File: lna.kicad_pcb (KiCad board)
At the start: 2 copper layers, 50.5 x 40.5 mm, 21 parts, among them P1 CONN_1, P2 CONN_2, P3 CONN_1, P4 CONN_1, Q1 BFG540W, U1 LM7810CT

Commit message: Optimizes the layout
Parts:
- Q1: footprint w_smd_trans:sot143B -> bfg540w:sot143B
- moved C3 11.7 mm to (125.1, 116.2), turned to 180 degrees
- moved L2 5.99 mm to (135.3, 106.7), turned to 0 degrees
- moved C1 5.12 mm to (125.1, 106.7), turned to 180 degrees
- moved C2 4.07 mm to (128.9, 94.0)
- moved U1 4.07 mm to (137.2, 95.9)
- moved R3 3.24 mm to (148.0, 104.8)
- moved L3 3.18 mm to (145.4, 108.0)
- moved C5 3.17 mm to (145.4, 94.0)
- moved C6 1.80 mm to (145.4, 111.8)
- moved R1 1.80 mm to (141.0, 111.8)
- moved R2 1.80 mm to (143.5, 111.8)
- moved P2 1.27 mm to (118.1, 94.0)
- moved C4 0.90 mm to (134.0, 112.4), turned to 270 degrees
- moved L1 0.90 mm to (128.9, 112.4), turned to 270 degrees
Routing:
- net GND: track 5.00 -> 164.1 mm
- net Net-(C4-Pad1): track 8.57 -> 3.52 mm
- net Net-(C1-Pad2): track 9.33 -> 4.73 mm
- net Net-(C8-Pad2): track 8.32 -> 4.00 mm
- net Net-(C6-Pad2): track 19.1 -> 15.3 mm
- net VCC: track 16.5 -> 19.6 mm
- net Net-(C1-Pad1): track 8.57 -> 5.77 mm
- net Net-(L2-Pad2): track 9.14 -> 11.2 mm
- net Net-(C3-Pad1): track 10.1 -> 12.0 mm
- net (no net): track 1.61 -> 0.00 mm, vias 1 -> 0

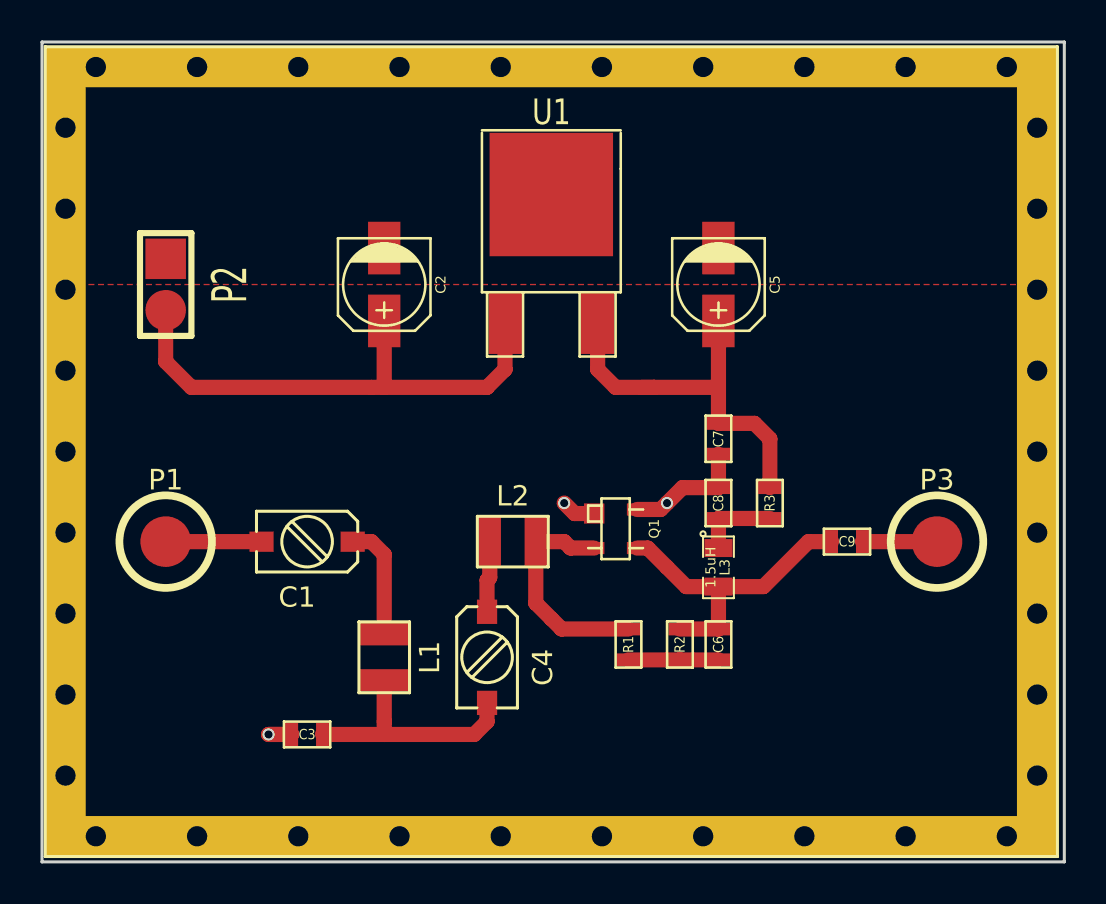
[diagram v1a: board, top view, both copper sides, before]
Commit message: Those are called LC filters not CL filters ... D'oh
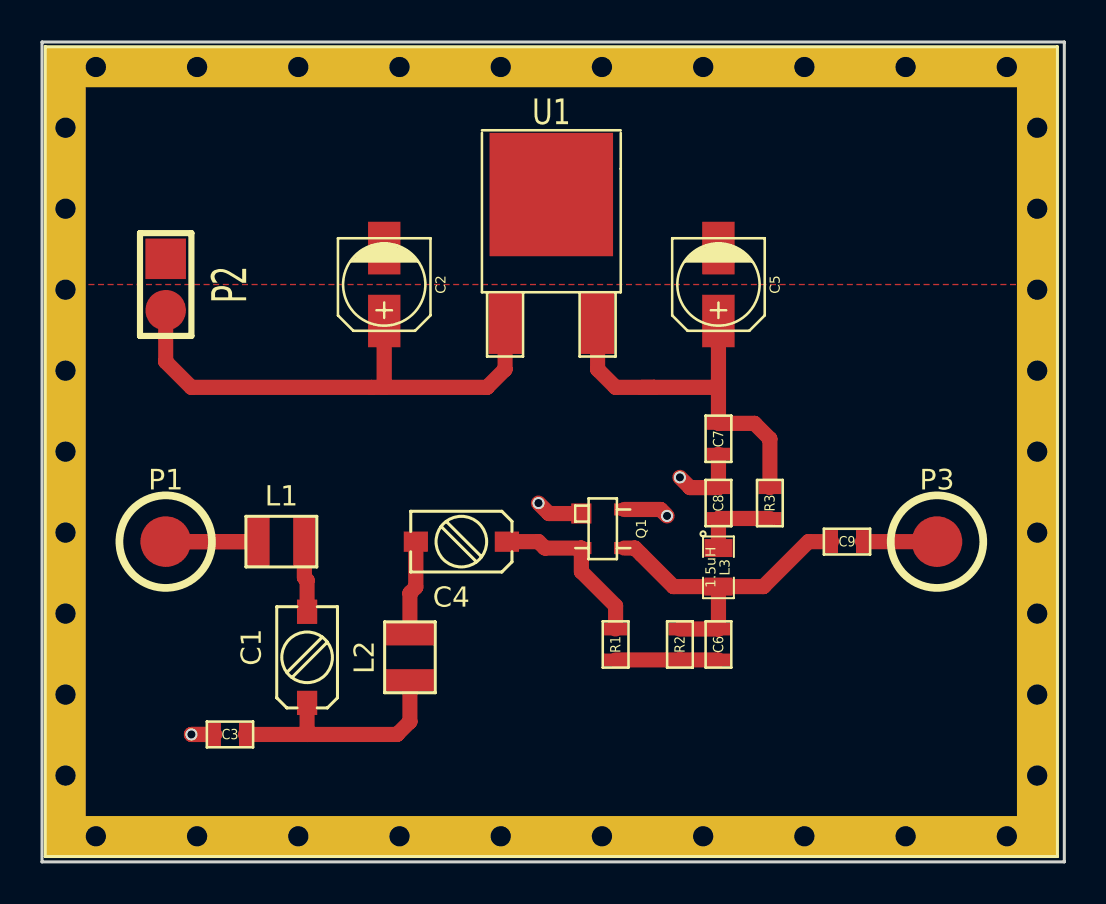
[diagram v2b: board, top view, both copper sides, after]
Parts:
- L1, L2: value 400nH -> 470nH
- moved L1 7.65 mm to (123.8, 106.7), turned to 0 degrees
- moved L2 7.65 mm to (130.2, 112.4), turned to 90 degrees
- moved C4 5.85 mm to (132.7, 106.7), turned to 180 degrees
- moved C1 5.71 mm to (125.1, 112.4), turned to 90 degrees
- moved C3 3.81 mm to (121.3, 116.2)
- moved Q1 0.64 mm to (139.7, 106.0)
- moved R1 0.63 mm to (140.3, 111.8)
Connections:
- C3 pad 1: Net-(C3-Pad1) -> Net-(C1-Pad1)
- C4 pad 2: Net-(C3-Pad1) -> Net-(C4-Pad2)
- L1 pad 1: Net-(C1-Pad1) -> Net-(L1-Pad1)
- L1 pad 2: Net-(C3-Pad1) -> Net-(C1-Pad2)
- L2 pad 1: Net-(C4-Pad1) -> Net-(C1-Pad1)
- L2 pad 2: Net-(L2-Pad2) -> Net-(C4-Pad2)
- P1 pad 1: Net-(C1-Pad2) -> Net-(L1-Pad1)
- Q1 pad 2: Net-(L2-Pad2) -> Net-(C4-Pad1)
- R1 pad 2: Net-(L2-Pad2) -> Net-(C4-Pad1)
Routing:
- net GND: track 164.1 -> 10.6 mm, vias 3 -> 4
- net Net-(C3-Pad1): track 12.0 -> 0.00 mm
- net Net-(L2-Pad2): track 11.2 -> 0.00 mm
- net Net-(L1-Pad1): track 0.00 -> 8.53 mm
- net Net-(C1-Pad1): track 5.77 -> 12.0 mm
- net Net-(C4-Pad1): track 3.52 -> 8.51 mm
- net Net-(C4-Pad2): track 0.00 -> 4.70 mm
- net Net-(C1-Pad2): track 4.73 -> 3.52 mm
- net Net-(C6-Pad1): track 4.44 -> 5.08 mm
- net Net-(C6-Pad2): track 15.3 -> 16.0 mm

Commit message: This might be 50Ohm
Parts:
- moved R3 4.58 mm to (145.4, 101.0)
- moved L3 3.81 mm to (145.4, 104.1)
- moved C8 3.24 mm to (148.6, 104.1), turned to 180 degrees
- moved C7 3.24 mm to (148.6, 101.0), turned to 180 degrees
- moved R1 2.69 mm to (138.4, 109.9)
- moved C1 1.91 mm to (127.0, 112.4)
- moved C6 1.91 mm to (145.4, 109.9)
- moved R2 1.91 mm to (143.5, 109.9)
- moved Q1 1.57 mm to (141.2, 105.7)
- moved C4 1.42 mm to (131.4, 106.0), turned to 270 degrees
- moved L2 1.27 mm to (131.4, 112.4)
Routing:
- net Net-(C6-Pad1): track 5.08 -> 11.4 mm
- net Net-(C4-Pad1): track 8.51 -> 14.8 mm
- net Net-(L1-Pad1): track 8.53 -> 4.58 mm
- net VCC: track 19.6 -> 16.4 mm
- net Net-(C1-Pad1): track 12.0 -> 15.0 mm
- net GND: track 10.6 -> 13.5 mm, vias 4 -> 5
- net Net-(C1-Pad2): track 3.52 -> 6.14 mm
